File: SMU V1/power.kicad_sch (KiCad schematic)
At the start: 0 parts

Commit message: i forget what i changed
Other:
- added sheet 3V3 LDO (untitled.kicad_sch)
- added sheet 5V Buck (5V_buck.kicad_sch)
- added sheet VBATT Protection (vbatt_protection.kicad_sch)
- note added: "DCDC brick options: CRE1S1205SC: only 200mA, no 24V capabiltiy, really bad (8-10% load line regulation), 3$ NXJ1S1205MC-R7: only 200mA, no 24V capability, 10-12% reg, $3.55 ROE-1205S: 200mA, no 24V, like 15% regulation, $3.6 1769405241: 400mA, no 24v, 8-15% regulation, $5.64 MER1S1205SC: 200mA, no 24V, 4.5-5% regulation, $6.11"
- note added: "budget out half an amp @ 5V roughly for the whole board so 2.5W max"
- note added: "ok so im thinking i want to make a standard like isolated interface so i dont have to think about grounding, and so any like future boards can be daisychained without any thought, also so i can kill power line noise also to save board space and save from nuking efficiency, need it to be one module that goes 12-5V and then ideally can take up to 24v so ima do what guitar power supplies do to get r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"
- note added: "so we need a switcher module, a decent transformer, inductor, decent caps, and some way to bring feedback across galvanic boundary for the supply itself ideally some sorta pgood system... what else"

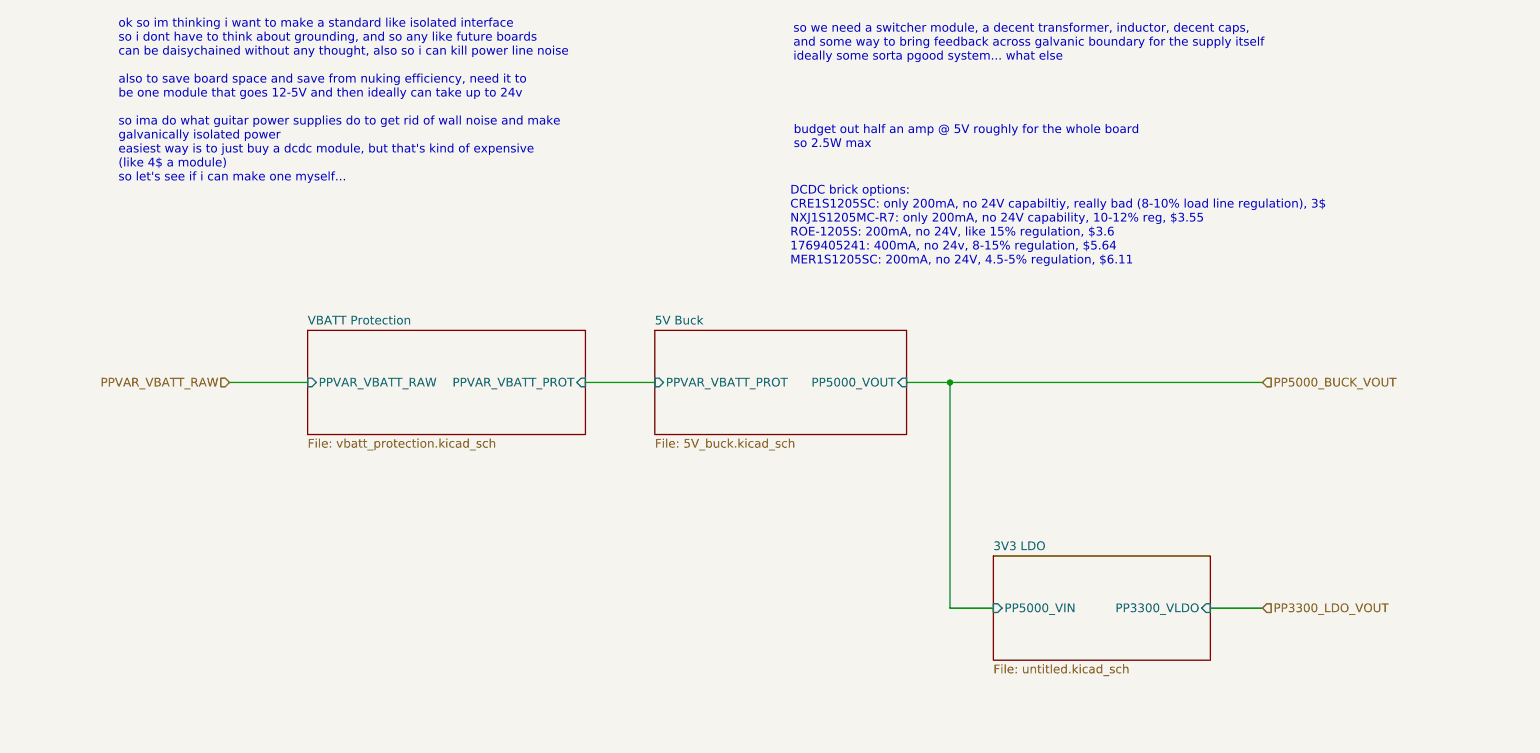
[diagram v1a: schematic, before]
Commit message: halfway done with routing, still needs antenna
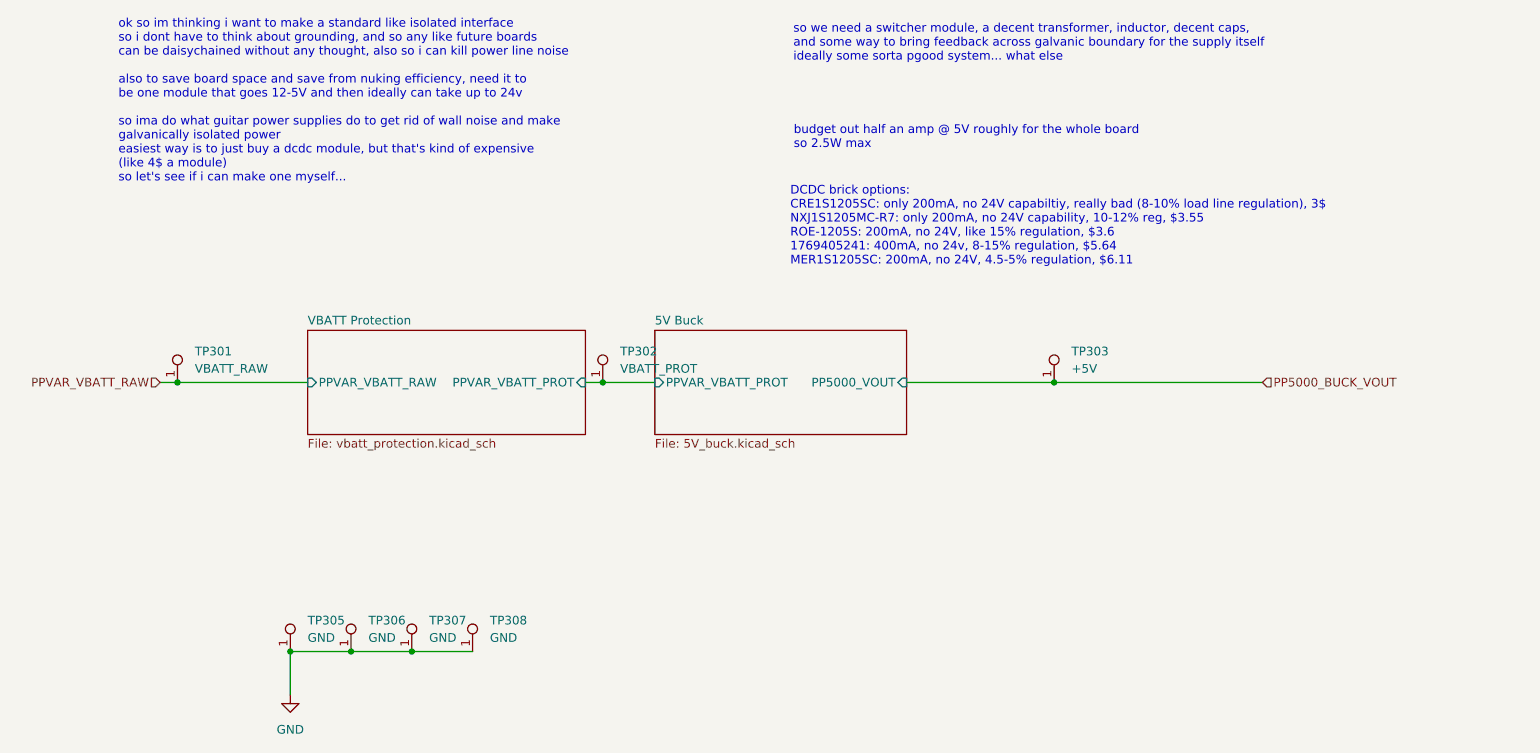
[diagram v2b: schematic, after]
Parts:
- added TP301: VBATT_RAW, bfr_utilities:TestPoint_Keystone_5019_Miniature, symbol bfr_utilities:SMD_Test_Point
- added TP302: VBATT_PROT, bfr_utilities:TestPoint_Keystone_5019_Miniature, symbol bfr_utilities:SMD_Test_Point
- added TP303: +5V, bfr_utilities:TestPoint_Keystone_5019_Miniature, symbol bfr_utilities:SMD_Test_Point
- added TP305, TP306, TP307, TP308: GND, bfr_utilities:TestPoint_Keystone_5019_Miniature, symbol bfr_utilities:SMD_Test_Point
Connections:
- net 5V Buck/PPVAR_VBATT_PROT: now also TP302.1
- net PP5000_BUCK_VOUT: now also TP303.1
- net PPVAR_VBATT_RAW: now also TP301.1
- new net GND: TP305.1, TP306.1, TP307.1, TP308.1
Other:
- removed sheet 3V3 LDO
